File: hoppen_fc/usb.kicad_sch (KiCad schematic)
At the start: 10 parts, among them J1 USB_C_Receptacle_USB2.0_16P, U5 USBLC6-2SC6

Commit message: work
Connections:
- net USB_PRE_TVS_N is gone; now on net USB_NT_N: J1.A7 (D-), J1.B7 (D-), U5.1 (I/O1)
- net USB_PRE_TVS_P is gone; now on net USB_NT_P: J1.A6 (D+), J1.B6 (D+), U5.3 (I/O2)
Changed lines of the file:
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@@
 		)
 	)
-	(label "USB_PRE_TVS_P"
+	(label "USB_NT_P"
 		(at 139.7 111.76 0)
 		(effects
@@
 		)
 	)
-	(label "USB_PRE_TVS_N"
+	(label "USB_NT_N"
 		(at 139.7 104.14 0)
 		(effects

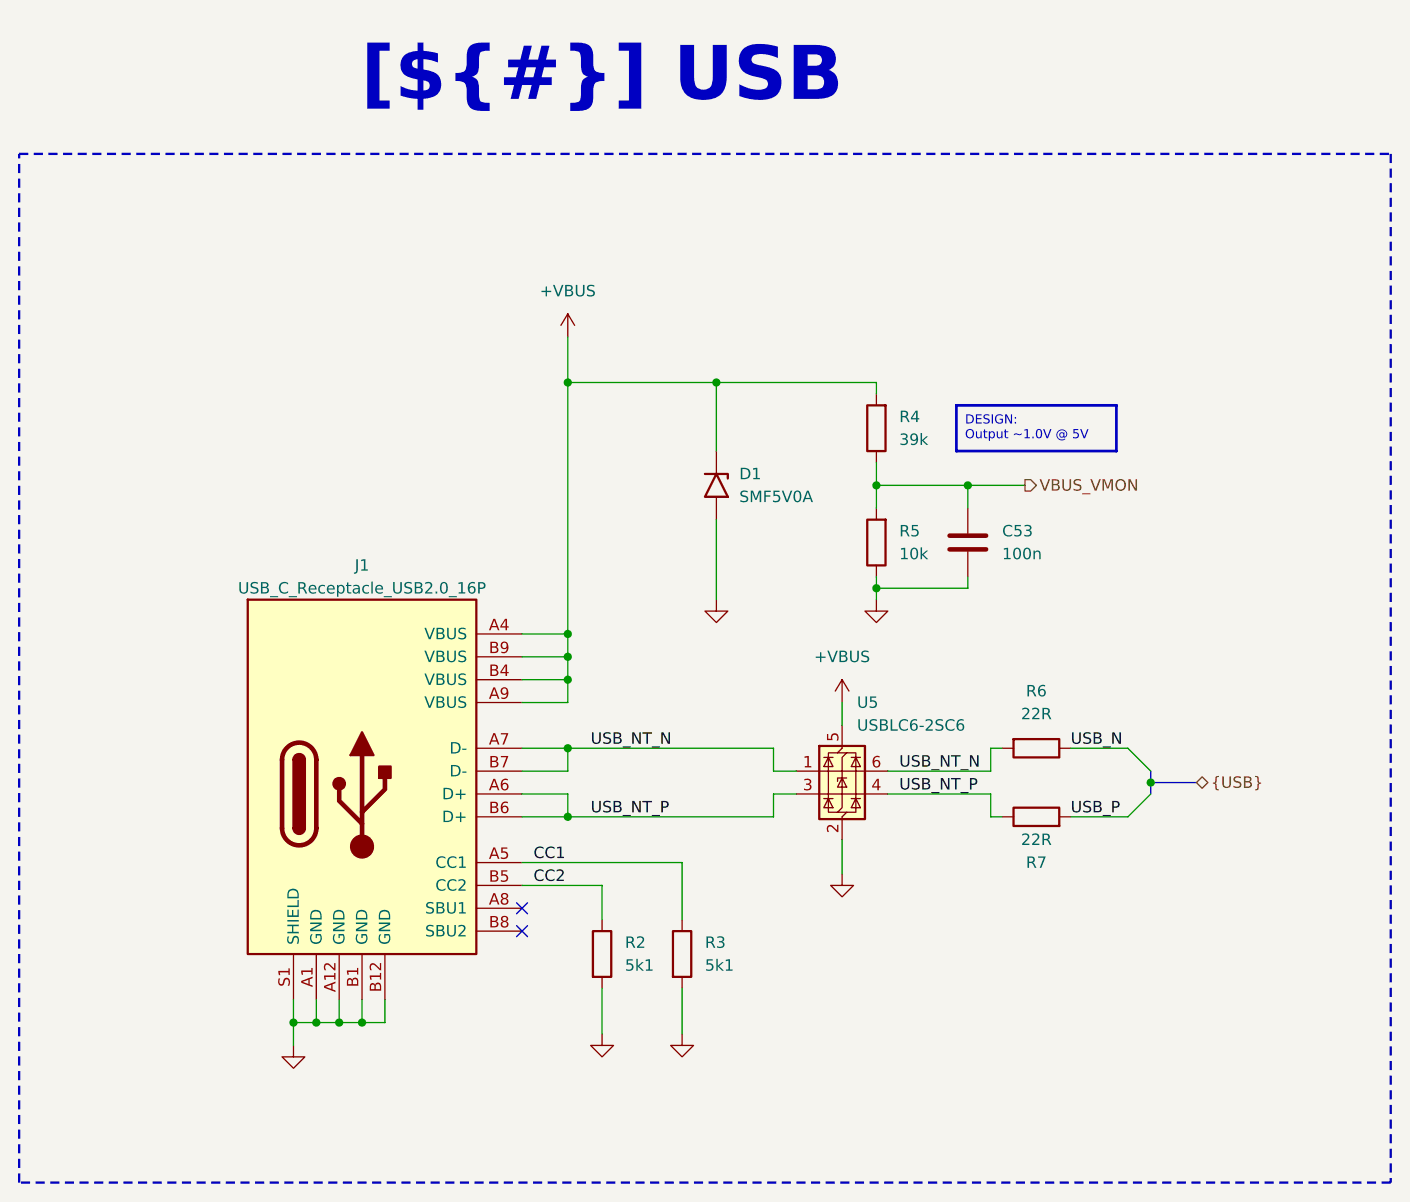
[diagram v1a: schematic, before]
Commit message: finished adding lcsc numbers
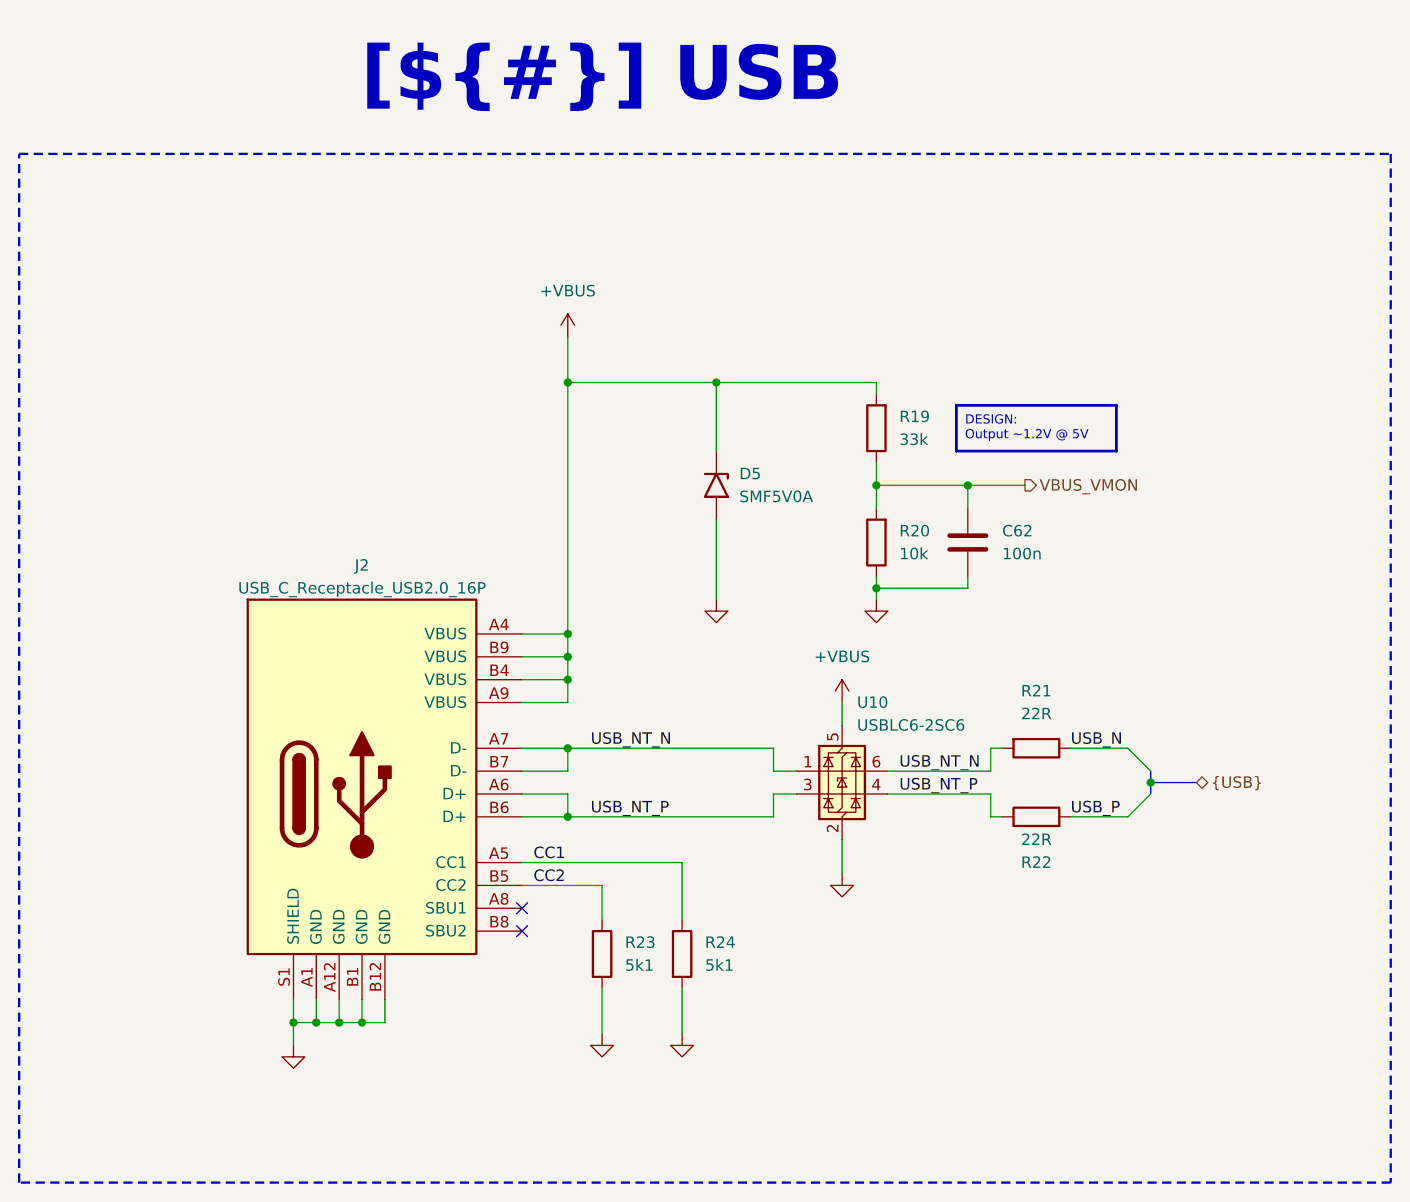
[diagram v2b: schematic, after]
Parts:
- C62: renamed from C53; LCSC (none) -> C307331
- D5: renamed from D1; LCSC (none) -> C1972946
- R19: renamed from R4; value 39k -> 33k; LCSC (none) -> C25779
- R20: renamed from R5; LCSC (none) -> C25744
- R21: renamed from R6; LCSC (none) -> C25092
- R22: renamed from R7; LCSC (none) -> C25092
- R23: renamed from R2; LCSC (none) -> C25905
- R24: renamed from R3; LCSC (none) -> C25905
- U10: renamed from U5; LCSC (none) -> C7519
- renumbered J1 to J2
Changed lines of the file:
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@@
 		)
 	)
-	(text_box "DESIGN:\nOutput ~1.0V @ 5V"
+	(text_box "DESIGN:\nOutput ~1.2V @ 5V"
 		(exclude_from_sim no)
 		(at 180.34 66.04 0)
@@
 		(dnp no)
 		(fields_autoplaced yes)
-		(property "Reference" "R3"
+		(property "Reference" "R24"
 			(at 152.4 125.7299 0)
 			(effects
@@
 		)
 		(property "Description" "Resistor"
+			(at 149.86 127 0)
+			(effects
+				(font
+					(size 1.27 1.27)
+				)
+				(hide yes)
+			)
+		)
+		(property "LCSC" "C25905"
 			(at 149.86 127 0)
 			(effects
@@
 			(project "hoppen_fc"
 				(path "/abe950a1-9eef-4508-9fd4-31d3e723e029/c85454e5-a89e-41eb-a5ed-71b4fc4cf13a/70185383-c6d2-4eb6-9764-fd02002b35f8"
-					(reference "R3")
+					(reference "R24")
 					(unit 1)
 				)
@@
 		(dnp no)
 		(fields_autoplaced yes)
-		(property "Reference" "R2"
+		(property "Reference" "R23"
 			(at 143.51 125.7299 0)
 			(effects
@@
 		)
 		(property "Description" "Resistor"
+			(at 140.97 127 0)
+			(effects
+				(font
+					(size 1.27 1.27)
+				)
+				(hide yes)
+			)
+		)
+		(property "LCSC" "C25905"
 			(at 140.97 127 0)
 			(effects
@@
 			(project ""
 				(path "/abe950a1-9eef-4508-9fd4-31d3e723e029/c85454e5-a89e-41eb-a5ed-71b4fc4cf13a/70185383-c6d2-4eb6-9764-fd02002b35f8"
-					(reference "R2")
+					(reference "R23")
 					(unit 1)
 				)
@@
 		(dnp no)
 		(fields_autoplaced yes)
-		(property "Reference" "U5"
+		(property "Reference" "U10"
 			(at 169.2911 99.06 0)
 			(effects
@@
 		(property "Description" "Very low capacitance ESD protection diode, 2 data-line, SOT-23-6"
 			(at 167.64 87.63 0)
+			(effects
+				(font
+					(size 1.27 1.27)
+				)
+				(hide yes)
+			)
+		)
+		(property "LCSC" "C7519"
+			(at 167.64 106.68 0)
 			(effects
 				(font
@@
 			(project ""
 				(path "/abe950a1-9eef-4508-9fd4-31d3e723e029/c85454e5-a89e-41eb-a5ed-71b4fc4cf13a/70185383-c6d2-4eb6-9764-fd02002b35f8"
-					(reference "U5")
+					(reference "U10")
 					(unit 1)
 				)
@@
 		(on_board yes)
 		(dnp no)
-		(property "Reference" "J1"
+		(property "Reference" "J2"
 			(at 114.3 83.82 0)
 			(effects
@@
 			(project ""
 				(path "/abe950a1-9eef-4508-9fd4-31d3e723e029/c85454e5-a89e-41eb-a5ed-71b4fc4cf13a/70185383-c6d2-4eb6-9764-fd02002b35f8"
-					(reference "J1")
+					(reference "J2")
 					(unit 1)
 				)
@@
 		(dnp no)
 		(fields_autoplaced yes)
-		(property "Reference" "#PWR036"
+		(property "Reference" "#PWR087"
 			(at 140.97 142.24 0)
 			(effects
@@
 			(project "hoppen_fc"
 				(path "/abe950a1-9eef-4508-9fd4-31d3e723e029/c85454e5-a89e-41eb-a5ed-71b4fc4cf13a/70185383-c6d2-4eb6-9764-fd02002b35f8"
-					(reference "#PWR036")
+					(reference "#PWR087")
 					(unit 1)
 				)
@@
 		(on_board yes)
 		(dnp no)
-		(property "Reference" "#PWR038"
+		(property "Reference" "#PWR085"
 			(at 167.64 102.87 0)
 			(effects
@@
 			(project "hoppen_fc"
 				(path "/abe950a1-9eef-4508-9fd4-31d3e723e029/c85454e5-a89e-41eb-a5ed-71b4fc4cf13a/70185383-c6d2-4eb6-9764-fd02002b35f8"
-					(reference "#PWR038")
+					(reference "#PWR085")
 					(unit 1)
 				)
@@
 		(dnp no)
 		(fields_autoplaced yes)
-		(property "Reference" "C53"
+		(property "Reference" "C62"
 			(at 185.42 80.0099 0)
 			(effects
@@
 		)
 		(property "Description" "Unpolarized capacitor"
+			(at 181.61 81.28 0)
+			(effects
+				(font
+					(size 1.27 1.27)
+				)
+				(hide yes)
+			)
+		)
+		(property "LCSC" "C307331"
 			(at 181.61 81.28 0)
 			(effects
@@
 			(project "hoppen_fc"
 				(path "/abe950a1-9eef-4508-9fd4-31d3e723e029/c85454e5-a89e-41eb-a5ed-71b4fc4cf13a/70185383-c6d2-4eb6-9764-fd02002b35f8"
-					(reference "C53")
+					(reference "C62")
 					(unit 1)
 				)
@@
 		(dnp no)
 		(fields_autoplaced yes)
-		(property "Reference" "D1"
+		(property "Reference" "D5"
 			(at 156.21 73.6599 90)
 			(effects
@@
 		(property "Description" "200W unidirectional Transil Transient Voltage Suppressor, 5Vrwm, SMF"
 			(at 165.1 74.93 0)
+			(effects
+				(font
+					(size 1.27 1.27)
+				)
+				(hide yes)
+			)
+		)
+		(property "LCSC" "C1972946"
+			(at 153.67 74.93 90)
 			(effects
 				(font
@@
 			(project "hoppen_fc"
 				(path "/abe950a1-9eef-4508-9fd4-31d3e723e029/c85454e5-a89e-41eb-a5ed-71b4fc4cf13a/70185383-c6d2-4eb6-9764-fd02002b35f8"
-					(reference "D1")
+					(reference "D5")
 					(unit 1)
 				)
@@
 		(dnp no)
 		(fields_autoplaced yes)
-		(property "Reference" "#PWR037"
+		(property "Reference" "#PWR088"
 			(at 149.86 142.24 0)
 			(effects
@@
 			(project "hoppen_fc"
 				(path "/abe950a1-9eef-4508-9fd4-31d3e723e029/c85454e5-a89e-41eb-a5ed-71b4fc4cf13a/70185383-c6d2-4eb6-9764-fd02002b35f8"
-					(reference "#PWR037")
+					(reference "#PWR088")
 					(unit 1)
 				)
@@
 		(dnp no)
 		(fields_autoplaced yes)
-		(property "Reference" "R6"
+		(property "Reference" "R21"
 			(at 189.23 97.79 90)
 			(effects
@@
 		(property "Description" "Resistor"
 			(at 189.23 104.14 0)
+			(effects
+				(font
+					(size 1.27 1.27)
+				)
+				(hide yes)
+			)
+		)
+		(property "LCSC" "C25092"
+			(at 189.23 104.14 90)
 			(effects
 				(font
@@
 			(project "hoppen_fc"
 				(path "/abe950a1-9eef-4508-9fd4-31d3e723e029/c85454e5-a89e-41eb-a5ed-71b4fc4cf13a/70185383-c6d2-4eb6-9764-fd02002b35f8"
-					(reference "R6")
+					(reference "R21")
 					(unit 1)
 				)
@@
 		(dnp no)
 		(fields_autoplaced yes)
-		(property "Reference" "#PWR034"
+		(property "Reference" "#PWR089"
 			(at 106.68 143.51 0)
 			(effects
@@
 			(project "hoppen_fc"
 				(path "/abe950a1-9eef-4508-9fd4-31d3e723e029/c85454e5-a89e-41eb-a5ed-71b4fc4cf13a/70185383-c6d2-4eb6-9764-fd02002b35f8"
-					(reference "#PWR034")
+					(reference "#PWR089")
 					(unit 1)
 				)
@@
 		(dnp no)
 		(fields_autoplaced yes)
-		(property "Reference" "#PWR035"
+		(property "Reference" "#PWR082"
 			(at 137.16 62.23 0)
 			(effects
@@
 			(project "hoppen_fc"
 				(path "/abe950a1-9eef-4508-9fd4-31d3e723e029/c85454e5-a89e-41eb-a5ed-71b4fc4cf13a/70185383-c6d2-4eb6-9764-fd02002b35f8"
-					(reference "#PWR035")
+					(reference "#PWR082")
 					(unit 1)
 				)
@@
 		(dnp no)
 		(fields_autoplaced yes)
-		(property "Reference" "#PWR040"
+		(property "Reference" "#PWR084"
 			(at 171.45 93.98 0)
 			(effects
@@
 			(project "hoppen_fc"
 				(path "/abe950a1-9eef-4508-9fd4-31d3e723e029/c85454e5-a89e-41eb-a5ed-71b4fc4cf13a/70185383-c6d2-4eb6-9764-fd02002b35f8"
-					(reference "#PWR040")
+					(reference "#PWR084")
 					(unit 1)
 				)
@@
 		(dnp no)
 		(fields_autoplaced yes)
-		(property "Reference" "#PWR041"
+		(property "Reference" "#PWR083"
 			(at 153.67 93.98 0)
 			(effects
@@
 			(project "hoppen_fc"
 				(path "/abe950a1-9eef-4508-9fd4-31d3e723e029/c85454e5-a89e-41eb-a5ed-71b4fc4cf13a/70185383-c6d2-4eb6-9764-fd02002b35f8"
-					(reference "#PWR041")
+					(reference "#PWR083")
 					(unit 1)
 				)
@@
 		(on_board yes)
 		(dnp no)
-		(property "Reference" "R7"
+		(property "Reference" "R22"
 			(at 189.23 116.84 90)
 			(effects
@@
 		(property "Description" "Resistor"
 			(at 189.23 111.76 0)
+			(effects
+				(font
+					(size 1.27 1.27)
+				)
+				(hide yes)
+			)
+		)
+		(property "LCSC" "C25092"
+			(at 189.23 111.76 90)
 			(effects
 				(font
@@
 			(project "hoppen_fc"
 				(path "/abe950a1-9eef-4508-9fd4-31d3e723e029/c85454e5-a89e-41eb-a5ed-71b4fc4cf13a/70185383-c6d2-4eb6-9764-fd02002b35f8"
-					(reference "R7")
+					(reference "R22")
 					(unit 1)
 				)
@@
 		(dnp no)
 		(fields_autoplaced yes)
-		(property "Reference" "R5"
+		(property "Reference" "R20"
 			(at 173.99 80.0099 0)
 			(effects
@@
 		)
 		(property "Description" "Resistor"
+			(at 171.45 81.28 0)
+			(effects
+				(font
+					(size 1.27 1.27)
+				)
+				(hide yes)
+			)
+		)
+		(property "LCSC" "C25744"
 			(at 171.45 81.28 0)
 			(effects
@@
 			(project "hoppen_fc"
 				(path "/abe950a1-9eef-4508-9fd4-31d3e723e029/c85454e5-a89e-41eb-a5ed-71b4fc4cf13a/70185383-c6d2-4eb6-9764-fd02002b35f8"
-					(reference "R5")
+					(reference "R20")
 					(unit 1)
 				)
@@
 		(dnp no)
 		(fields_autoplaced yes)
-		(property "Reference" "R4"
+		(property "Reference" "R19"
 			(at 173.99 67.3099 0)
 			(effects
@@
 			)
 		)
-		(property "Value" "39k"
+		(property "Value" "33k"
 			(at 173.99 69.8499 0)
 			(effects
@@
 		)
 		(property "Description" "Resistor"
+			(at 171.45 68.58 0)
+			(effects
+				(font
+					(size 1.27 1.27)
+				)
+				(hide yes)
+			)
+		)
+		(property "LCSC" "C25779"
 			(at 171.45 68.58 0)
 			(effects
@@
 			(project "hoppen_fc"
 				(path "/abe950a1-9eef-4508-9fd4-31d3e723e029/c85454e5-a89e-41eb-a5ed-71b4fc4cf13a/70185383-c6d2-4eb6-9764-fd02002b35f8"
-					(reference "R4")
+					(reference "R19")
 					(unit 1)
 				)
@@
 		(dnp no)
 		(fields_autoplaced yes)
-		(property "Reference" "#PWR039"
+		(property "Reference" "#PWR086"
 			(at 167.64 124.46 0)
 			(effects
@@
 			(project "hoppen_fc"
 				(path "/abe950a1-9eef-4508-9fd4-31d3e723e029/c85454e5-a89e-41eb-a5ed-71b4fc4cf13a/70185383-c6d2-4eb6-9764-fd02002b35f8"
-					(reference "#PWR039")
+					(reference "#PWR086")
 					(unit 1)
 				)
